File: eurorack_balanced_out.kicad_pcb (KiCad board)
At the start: 2 copper layers, 60 x 35 mm, 31 parts, among them J1 Conn_01x02, J2 Conn_01x02, J3 Conn_02x05_Odd_Even, J4 AudioJack3, J5 AudioJack3, U1 THAT1646W16, U2 THAT1646W16

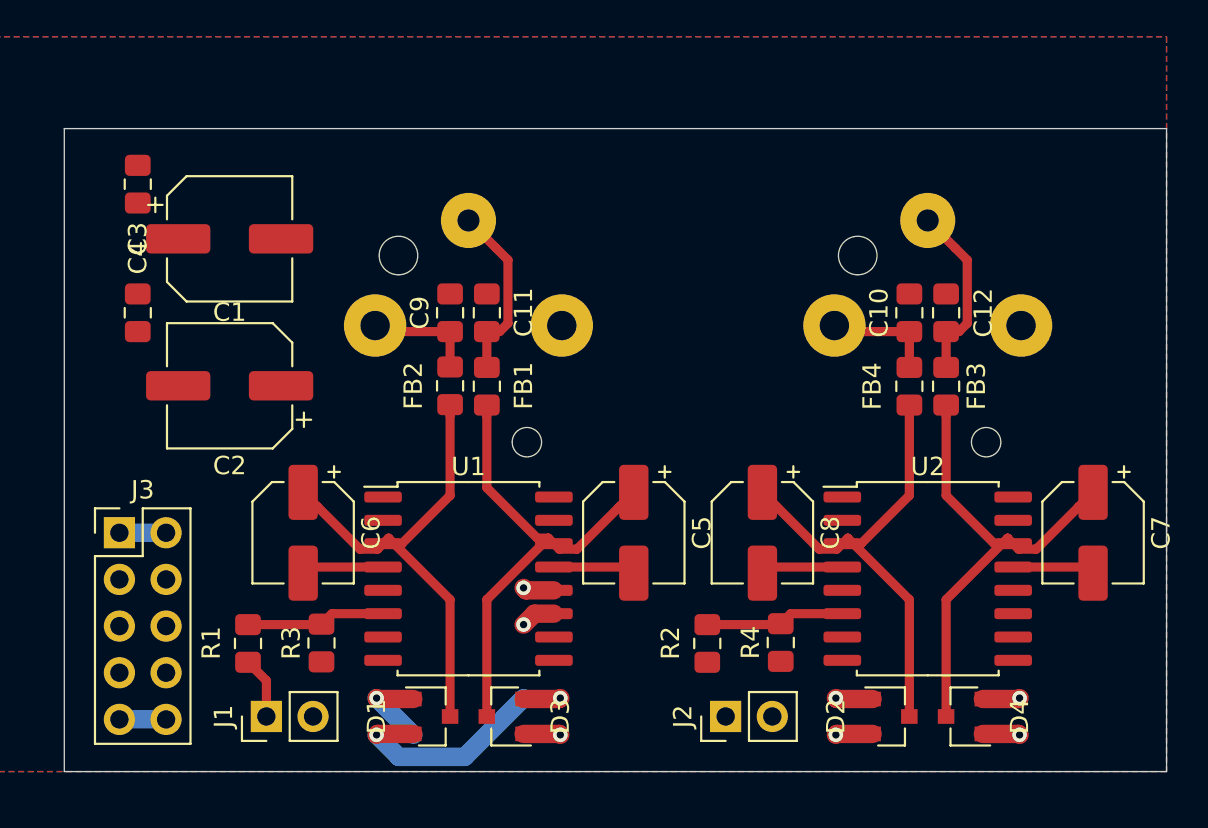
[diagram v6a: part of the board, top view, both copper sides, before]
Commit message: prepare for power routing and cleanup
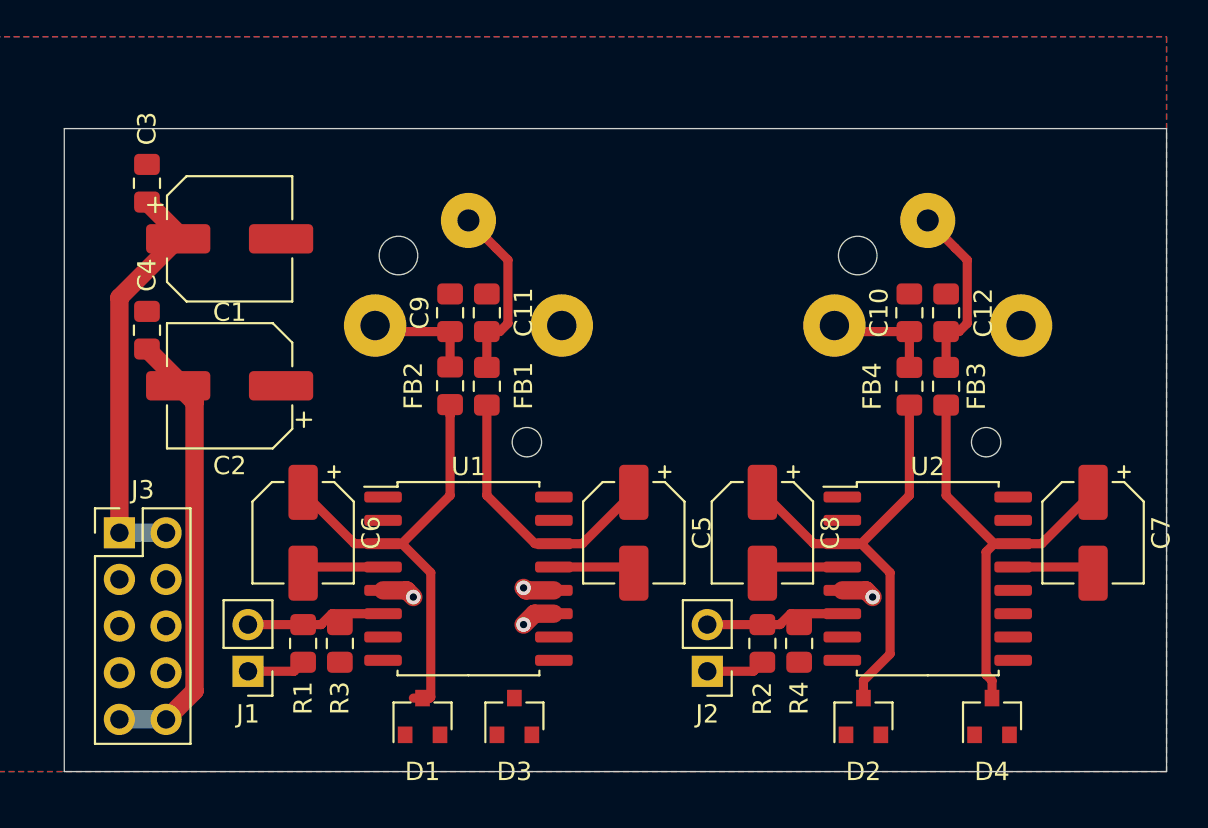
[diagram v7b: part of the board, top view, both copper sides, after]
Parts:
- moved R1 3.00 mm to (133.0, 143.0)
- moved R2 3.00 mm to (158.0, 143.0)
- moved J1 2.66 mm to (130.0, 144.5), turned to 180 degrees
- moved J2 2.66 mm to (155.0, 144.5), turned to 180 degrees
- moved D2 1.50 mm to (163.5, 147.0), turned to 90 degrees
- moved D4 1.50 mm to (170.5, 147.0), turned to 90 degrees
- moved C4 1.07 mm to (124.5, 126.0)
- moved R4 1.00 mm to (160.0, 143.0)
- moved R3 1.00 mm to (135.0, 143.0)
- moved C3 0.50 mm to (124.5, 118.0), turned to 270 degrees
- moved D1 0.50 mm to (139.5, 147.0), turned to 90 degrees
- moved D3 0.50 mm to (144.5, 147.0), turned to 90 degrees
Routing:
- net Net-(C5-Pad1): track 26.3 -> 15.2 mm
- net Vee: track 15.3 -> 26.3 mm, vias 5 -> 1
- net GND: track 0.00 -> 3.60 mm, vias 0 -> 2
- net Net-(J2-Pad1): track 0.00 -> 3.20 mm
- net Net-(C7-Pad1): track 26.9 -> 23.9 mm
- net Vcc: track 22.2 -> 24.3 mm, vias 5 -> 1
- net Net-(C8-Pad1): track 26.9 -> 24.8 mm
- net Net-(C6-Pad1): track 27.0 -> 25.2 mm
